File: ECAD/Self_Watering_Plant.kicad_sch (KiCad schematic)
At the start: 10 parts, among them J1 Conn_01x02, J2 Conn_01x02, J3 Conn_01x02, J4 Conn_01x02, J5 Conn_01x02, J6 USB_A, J7 Conn_01x02, J8 Conn_01x02, J9 Conn_01x03, P1 U262-161N-4BVC11

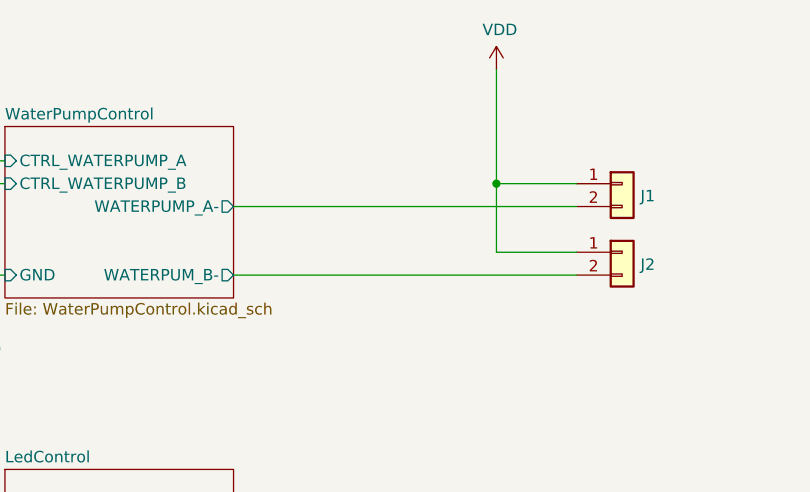
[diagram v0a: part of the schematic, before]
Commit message: pcb layout has started, still ned to make 5V to 3.3V power supply, add dip switch do individually control input power of each switch, 5V or 12V
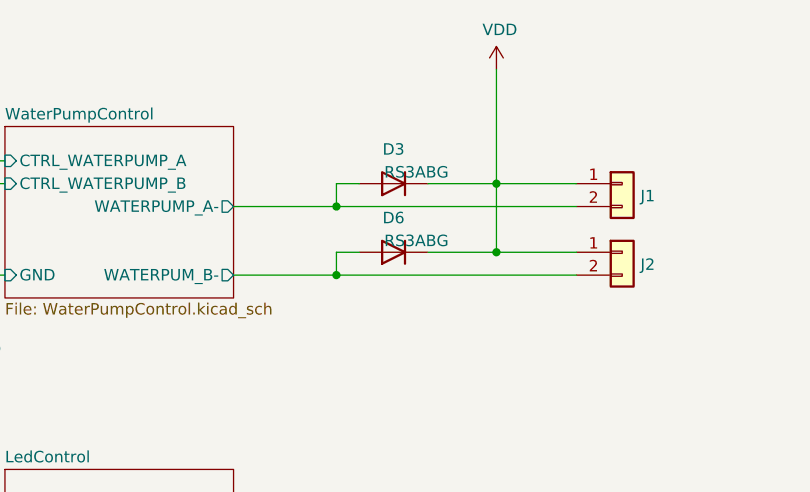
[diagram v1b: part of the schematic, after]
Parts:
- added D3, D6: RS3ABG, Diode_SMD:D_SMB, symbol Device:D
- J7, J8: footprint ConnectorsSMD:TB001-500-02BE -> Connector_JST:JST_XH_S2B-XH-A_1x02_P2.50mm_Horizontal
- J9: footprint (none) -> Connector_JST:JST_XH_S3B-XH-A_1x03_P2.50mm_Horizontal
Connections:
- net VDD: now also D3.1 (K), D6.1 (K)
- net WaterPumpControl/WATERPUMP_A-: now also D3.2 (A)
- net WaterPumpControl/WATERPUM_B-: now also D6.2 (A)
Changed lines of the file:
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@@
   (junction (at 44.45 166.37) (diameter 0.9144) (color 0 0 0 0))
   (junction (at 104.14 45.72) (diameter 0.9144) (color 0 0 0 0))
+  (junction (at 226.06 50.8) (diameter 0.9144) (color 0 0 0 0))
+  (junction (at 226.06 58.42) (diameter 0.9144) (color 0 0 0 0))
   (junction (at 243.84 48.26) (diameter 0.9144) (color 0 0 0 0))
+  (junction (at 243.84 55.88) (diameter 0.9144) (color 0 0 0 0))
   (junction (at 243.84 92.71) (diameter 0.9144) (color 0 0 0 0))
   (junction (at 243.84 100.33) (diameter 0.9144) (color 0 0 0 0))
@@
     (stroke (width 0) (type solid) (color 0 0 0 0))
   )
-  (wire (pts (xy 214.63 50.8) (xy 252.73 50.8))
-    (stroke (width 0) (type solid) (color 0 0 0 0))
-  )
-  (wire (pts (xy 214.63 58.42) (xy 252.73 58.42))
+  (wire (pts (xy 214.63 50.8) (xy 226.06 50.8))
+    (stroke (width 0) (type solid) (color 0 0 0 0))
+  )
+  (wire (pts (xy 214.63 58.42) (xy 226.06 58.42))
     (stroke (width 0) (type solid) (color 0 0 0 0))
   )
@@
   )
   (wire (pts (xy 223.52 138.43) (xy 259.08 138.43))
+    (stroke (width 0) (type solid) (color 0 0 0 0))
+  )
+  (wire (pts (xy 226.06 48.26) (xy 226.06 50.8))
+    (stroke (width 0) (type solid) (color 0 0 0 0))
+  )
+  (wire (pts (xy 226.06 50.8) (xy 252.73 50.8))
+    (stroke (width 0) (type solid) (color 0 0 0 0))
+  )
+  (wire (pts (xy 226.06 55.88) (xy 226.06 58.42))
+    (stroke (width 0) (type solid) (color 0 0 0 0))
+  )
+  (wire (pts (xy 226.06 58.42) (xy 252.73 58.42))
+    (stroke (width 0) (type solid) (color 0 0 0 0))
+  )
+  (wire (pts (xy 228.6 48.26) (xy 226.06 48.26))
+    (stroke (width 0) (type solid) (color 0 0 0 0))
+  )
+  (wire (pts (xy 228.6 55.88) (xy 226.06 55.88))
+    (stroke (width 0) (type solid) (color 0 0 0 0))
+  )
+  (wire (pts (xy 236.22 48.26) (xy 243.84 48.26))
+    (stroke (width 0) (type solid) (color 0 0 0 0))
+  )
+  (wire (pts (xy 236.22 55.88) (xy 243.84 55.88))
     (stroke (width 0) (type solid) (color 0 0 0 0))
   )
@@
     (pin "1")
   )
+  (symbol (lib_id "Device:D") (at 232.41 48.26 180) (unit 1)
+    (in_bom yes) (on_board yes)
+    (property "Reference" "D3" (id 0) (at 232.41 44.45 0))
+    (property "Value" "RS3ABG" (id 1) (at 234.95 46.99 0))
+    (property "Footprint" "Diode_SMD:D_SMB" (id 2) (at 232.41 48.26 0)
+      (effects (font (size 1.27 1.27)) hide)
+    )
+    (property "Datasheet" "~" (id 3) (at 232.41 48.26 0)
+      (effects (font (size 1.27 1.27)) hide)
+    )
+    (pin "1")
+    (pin "2")
+  )
+  (symbol (lib_id "Device:D") (at 232.41 55.88 180) (unit 1)
+    (in_bom yes) (on_board yes)
+    (property "Reference" "D6" (id 0) (at 232.41 52.07 0))
+    (property "Value" "RS3ABG" (id 1) (at 234.95 54.61 0))
+    (property "Footprint" "Diode_SMD:D_SMB" (id 2) (at 232.41 55.88 0)
+      (effects (font (size 1.27 1.27)) hide)
+    )
+    (property "Datasheet" "~" (id 3) (at 232.41 55.88 0)
+      (effects (font (size 1.27 1.27)) hide)
+    )
+    (pin "1")
+    (pin "2")
+  )
   (symbol (lib_id "Connector_Generic:Conn_01x02") (at 34.29 120.65 0) (mirror y) (unit 1)
     (in_bom yes) (on_board yes)
@@
       (effects (font (size 1.27 1.27)) (justify left) hide)
     )
-    (property "Footprint" "ConnectorsSMD:TB001-500-02BE" (id 2) (at 34.29 120.65 0)
+    (property "Footprint" "Connector_JST:JST_XH_S2B-XH-A_1x02_P2.50mm_Horizontal" (id 2) (at 34.29 120.65 0)
       (effects (font (size 1.27 1.27)) hide)
     )
@@
       (effects (font (size 1.27 1.27)) (justify left) hide)
     )
-    (property "Footprint" "ConnectorsSMD:TB001-500-02BE" (id 2) (at 34.29 127 0)
-      (effects (font (size 1.27 1.27)) hide)
-    )
-    (property "Datasheet" "~" (id 3) (at 34.29 127 0)
+    (property "Footprint" "Connector_JST:JST_XH_S2B-XH-A_1x02_P2.50mm_Horizontal" (id 2) (at 34.29 127 0)
+      (effects (font (size 1.27 1.27)) hide)
+    )
+    (property "Datasheet" "S2B-XH-A(LF)(SN)" (id 3) (at 34.29 127 0)
       (effects (font (size 1.27 1.27)) hide)
     )
@@
     (property "Reference" "J9" (id 0) (at 36.83 137.16 0))
     (property "Value" "Conn_01x03" (id 1) (at 36.83 139.7 0))
-    (property "Footprint" "" (id 2) (at 34.29 146.05 0)
-      (effects (font (size 1.27 1.27)) hide)
-    )
-    (property "Datasheet" "~" (id 3) (at 34.29 146.05 0)
+    (property "Footprint" "Connector_JST:JST_XH_S3B-XH-A_1x03_P2.50mm_Horizontal" (id 2) (at 34.29 146.05 0)
+      (effects (font (size 1.27 1.27)) hide)
+    )
+    (property "Datasheet" "S3B-XH-A(LF)(SN)" (id 3) (at 34.29 146.05 0)
       (effects (font (size 1.27 1.27)) hide)
     )
@@
       (reference "#PWR0148") (unit 1) (value "+3.3V") (footprint "")
     )
+    (path "/7f85a4a8-872d-449e-ac98-dcebf98be1f5"
+      (reference "D3") (unit 1) (value "RS3ABG") (footprint "Diode_SMD:D_SMB")
+    )
+    (path "/afe34e03-5c53-48e0-8bac-a90e23adbb67"
+      (reference "D6") (unit 1) (value "RS3ABG") (footprint "Diode_SMD:D_SMB")
+    )
     (path "/00000000-0000-0000-0000-0000609a6f5d"
       (reference "J1") (unit 1) (value "Conn_01x02") (footprint "ConnectorsSMD:TB001-500-02BE")
@@
     )
     (path "/e762fdda-6f63-47b2-8c8e-31bd3db59fa1"
-      (reference "J7") (unit 1) (value "Conn_01x02") (footprint "ConnectorsSMD:TB001-500-02BE")
+      (reference "J7") (unit 1) (value "Conn_01x02") (footprint "Connector_JST:JST_XH_S2B-XH-A_1x02_P2.50mm_Horizontal")
     )
     (path "/5ff3cd88-b345-4964-9476-0cf1ad690106"
-      (reference "J8") (unit 1) (value "Conn_01x02") (footprint "ConnectorsSMD:TB001-500-02BE")
+      (reference "J8") (unit 1) (value "Conn_01x02") (footprint "Connector_JST:JST_XH_S2B-XH-A_1x02_P2.50mm_Horizontal")
     )
     (path "/ae311982-fa4d-4e28-b525-c8aedb285d2b"
-      (reference "J9") (unit 1) (value "Conn_01x03") (footprint "")
+      (reference "J9") (unit 1) (value "Conn_01x03") (footprint "Connector_JST:JST_XH_S3B-XH-A_1x03_P2.50mm_Horizontal")
     )
     (path "/00000000-0000-0000-0000-000060945ca1"
@@
     )
     (path "/00000000-0000-0000-0000-0000609b7c65/00000000-0000-0000-0000-0000609be32c"
-      (reference "U1") (unit 1) (value "LM393") (footprint "Potentiometer_SMD:Potentiometer_Bourns_TC33X_Vertical")
+      (reference "U1") (unit 1) (value "LM293") (footprint "Package_SO:SO-8_3.9x4.9mm_P1.27mm")
     )
     (path "/00000000-0000-0000-0000-0000609b7c65/00000000-0000-0000-0000-0000609be3b0"
-      (reference "U1") (unit 2) (value "LM393") (footprint "Potentiometer_SMD:Potentiometer_Bourns_TC33X_Vertical")
+      (reference "U1") (unit 2) (value "LM293") (footprint "Package_SO:SO-8_3.9x4.9mm_P1.27mm")
     )
     (path "/00000000-0000-0000-0000-0000609b7c65/00000000-0000-0000-0000-0000609c4856"
-      (reference "U1") (unit 3) (value "LM393") (footprint "Potentiometer_SMD:Potentiometer_Bourns_TC33X_Vertical")
+      (reference "U1") (unit 3) (value "LM293") (footprint "Package_SO:SO-8_3.9x4.9mm_P1.27mm")
     )
     (path "/00000000-0000-0000-0000-000060a2b29e/f73dcfc6-db4c-4ef4-bbee-f3fe5812d316"
@@
       (reference "R11") (unit 1) (value "10K") (footprint "Resistor_SMD:R_0603_1608Metric")
     )
-    (path "/00000000-0000-0000-0000-000060a2b29e/2c6267fd-e2e4-4818-99f8-f7a23991ac84"
-      (reference "R12") (unit 1) (value "10K") (footprint "Resistor_SMD:R_0603_1608Metric")
-    )
     (path "/00000000-0000-0000-0000-000060a2b29e/989751c3-4da0-4a0b-b582-c885a50d34a8"
       (reference "R14") (unit 1) (value "10K") (footprint "Resistor_SMD:R_0603_1608Metric")
@@
       (reference "RV4") (unit 1) (value "10K") (footprint "Potentiometer_SMD:Potentiometer_Bourns_TC33X_Vertical")
     )
+    (path "/00000000-0000-0000-0000-000060a2b29e/4583c5f5-b989-49ed-b260-0239b8493054"
+      (reference "U8") (unit 1) (value "LM293") (footprint "Package_SO:SO-8_3.9x4.9mm_P1.27mm")
+    )
+    (path "/00000000-0000-0000-0000-000060a2b29e/3f876a91-8f50-47a9-a5c1-7f531880fa14"
+      (reference "U8") (unit 2) (value "LM293") (footprint "Package_SO:SO-8_3.9x4.9mm_P1.27mm")
+    )
     (path "/00000000-0000-0000-0000-000060a2b29e/1afe9b1a-d1d5-441b-81fd-7e26b7468ac6"
-      (reference "U2") (unit 3) (value "LM393") (footprint "Potentiometer_SMD:Potentiometer_Bourns_TC33X_Vertical")
-    )
-    (path "/00000000-0000-0000-0000-000060a2b29e/4583c5f5-b989-49ed-b260-0239b8493054"
-      (reference "U8") (unit 1) (value "LM393") (footprint "Potentiometer_SMD:Potentiometer_Bourns_TC33X_Vertical")
-    )
-    (path "/00000000-0000-0000-0000-000060a2b29e/3f876a91-8f50-47a9-a5c1-7f531880fa14"
-      (reference "U8") (unit 2) (value "LM393") (footprint "Potentiometer_SMD:Potentiometer_Bourns_TC33X_Vertical")
+      (reference "U8") (unit 3) (value "LM293") (footprint "Package_SO:SO-8_3.9x4.9mm_P1.27mm")
     )
     (path "/00000000-0000-0000-0000-000060a212ac/00000000-0000-0000-0000-000060a221d1"
